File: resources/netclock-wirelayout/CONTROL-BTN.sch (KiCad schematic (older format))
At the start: 5 parts, among them J3 CNTRL, SW1 12.5mm Push Switch, SW2 12.5mm Push Switch

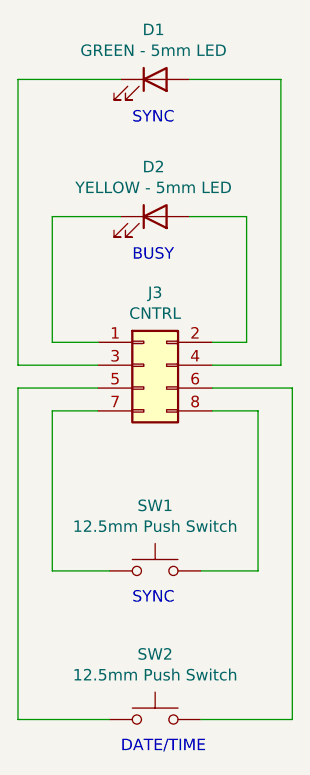
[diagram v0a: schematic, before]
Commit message: Update 7-segment display details in the wiring layout.
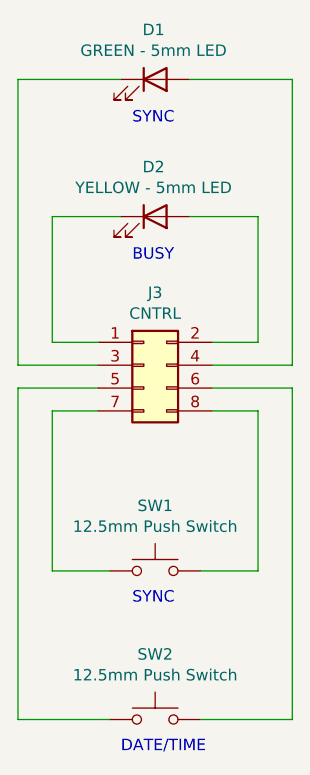
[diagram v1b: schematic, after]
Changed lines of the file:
@@
 $EndComp
-Wire Wire Line
-	6000 3400 6150 3400
-Wire Wire Line
-	6150 3400 6150 2850
-Wire Wire Line
-	6150 2850 5900 2850
 Wire Wire Line
 	5500 3400 5300 3400
@@
 Wire Wire Line
 	5300 2850 5600 2850
-Wire Wire Line
-	6000 3500 6300 3500
-Wire Wire Line
-	6300 3500 6300 2250
-Wire Wire Line
-	6300 2250 5900 2250
 Wire Wire Line
 	5500 3500 5150 3500
@@
 Text Notes 5650 4550 0    50   ~ 0
 SYNC
+Wire Wire Line
+	6200 3400 6200 2850
+Wire Wire Line
+	6000 3400 6200 3400
+Wire Wire Line
+	5900 2850 6200 2850
+Wire Wire Line
+	6350 2250 6350 3500
+Wire Wire Line
+	6000 3500 6350 3500
+Wire Wire Line
+	5900 2250 6350 2250
 $EndSCHEMATC
